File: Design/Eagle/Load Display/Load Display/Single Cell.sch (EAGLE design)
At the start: 12 parts

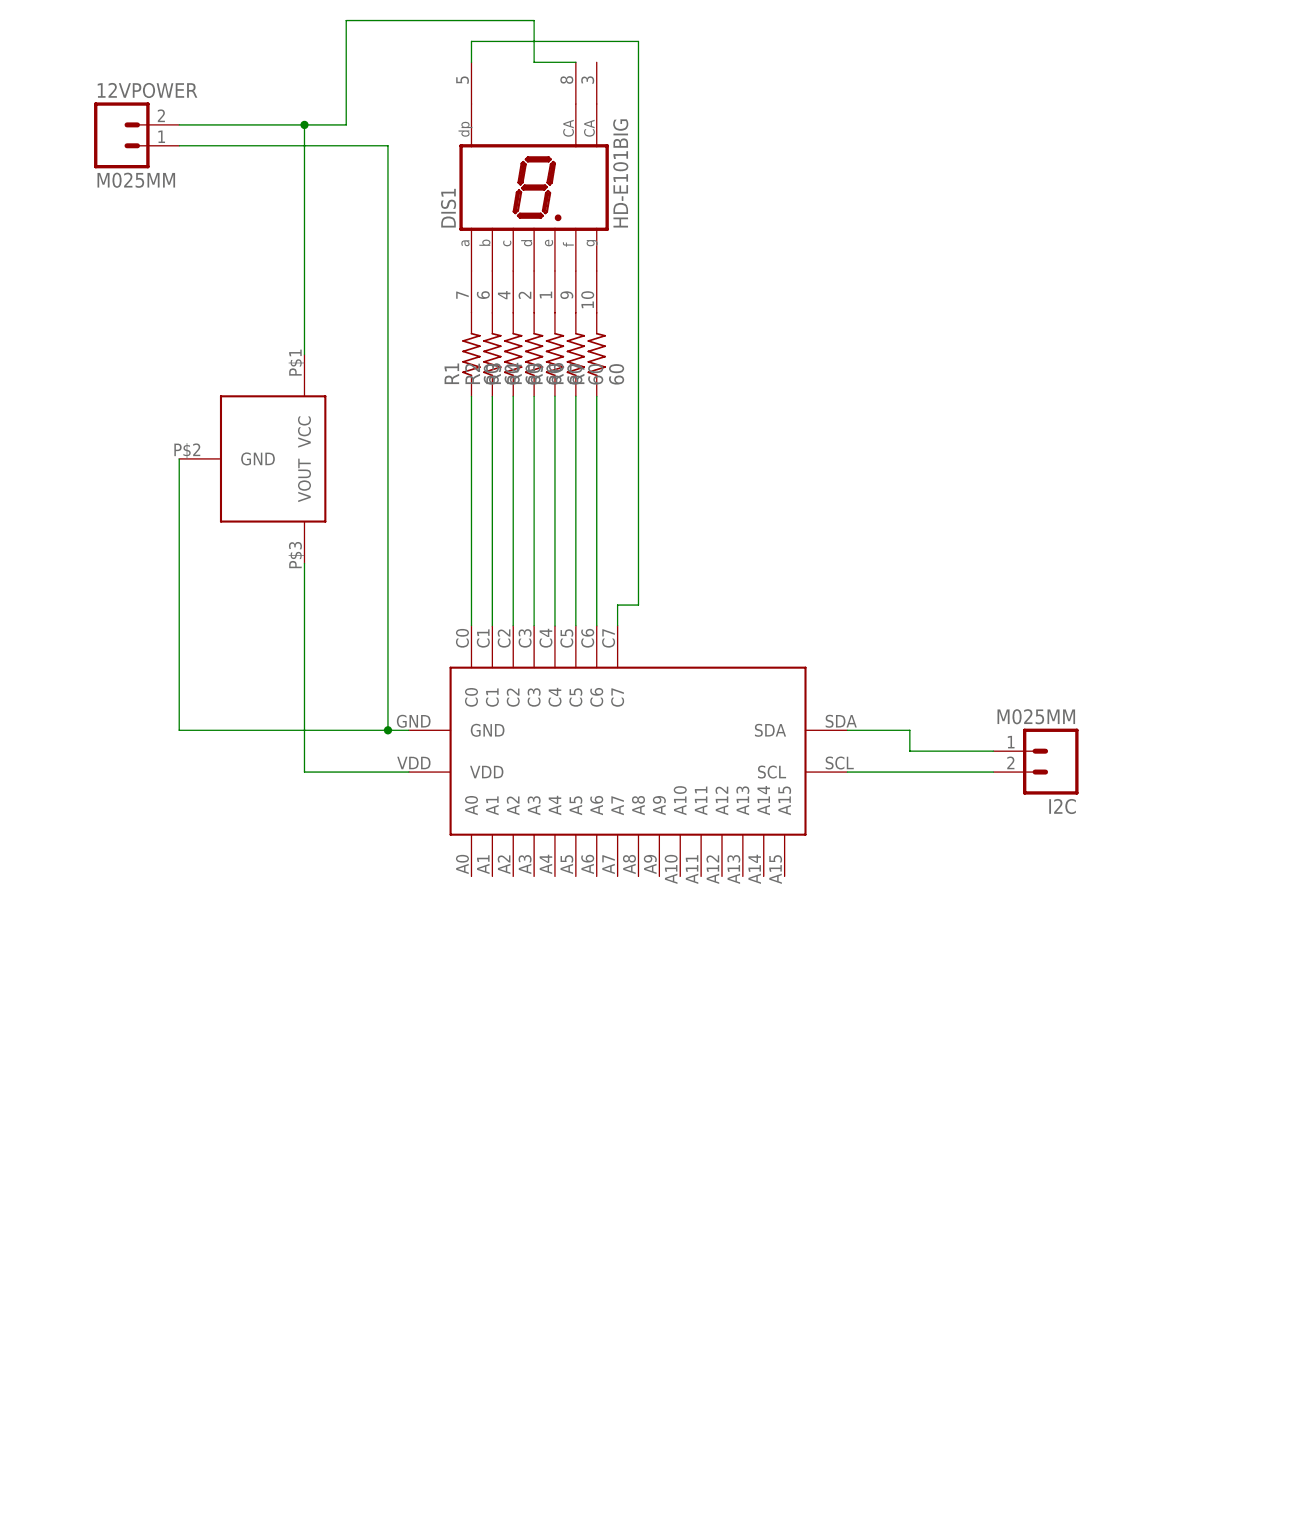
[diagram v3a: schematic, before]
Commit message: Added a bunch of stuff to make the new 7 segment boards.
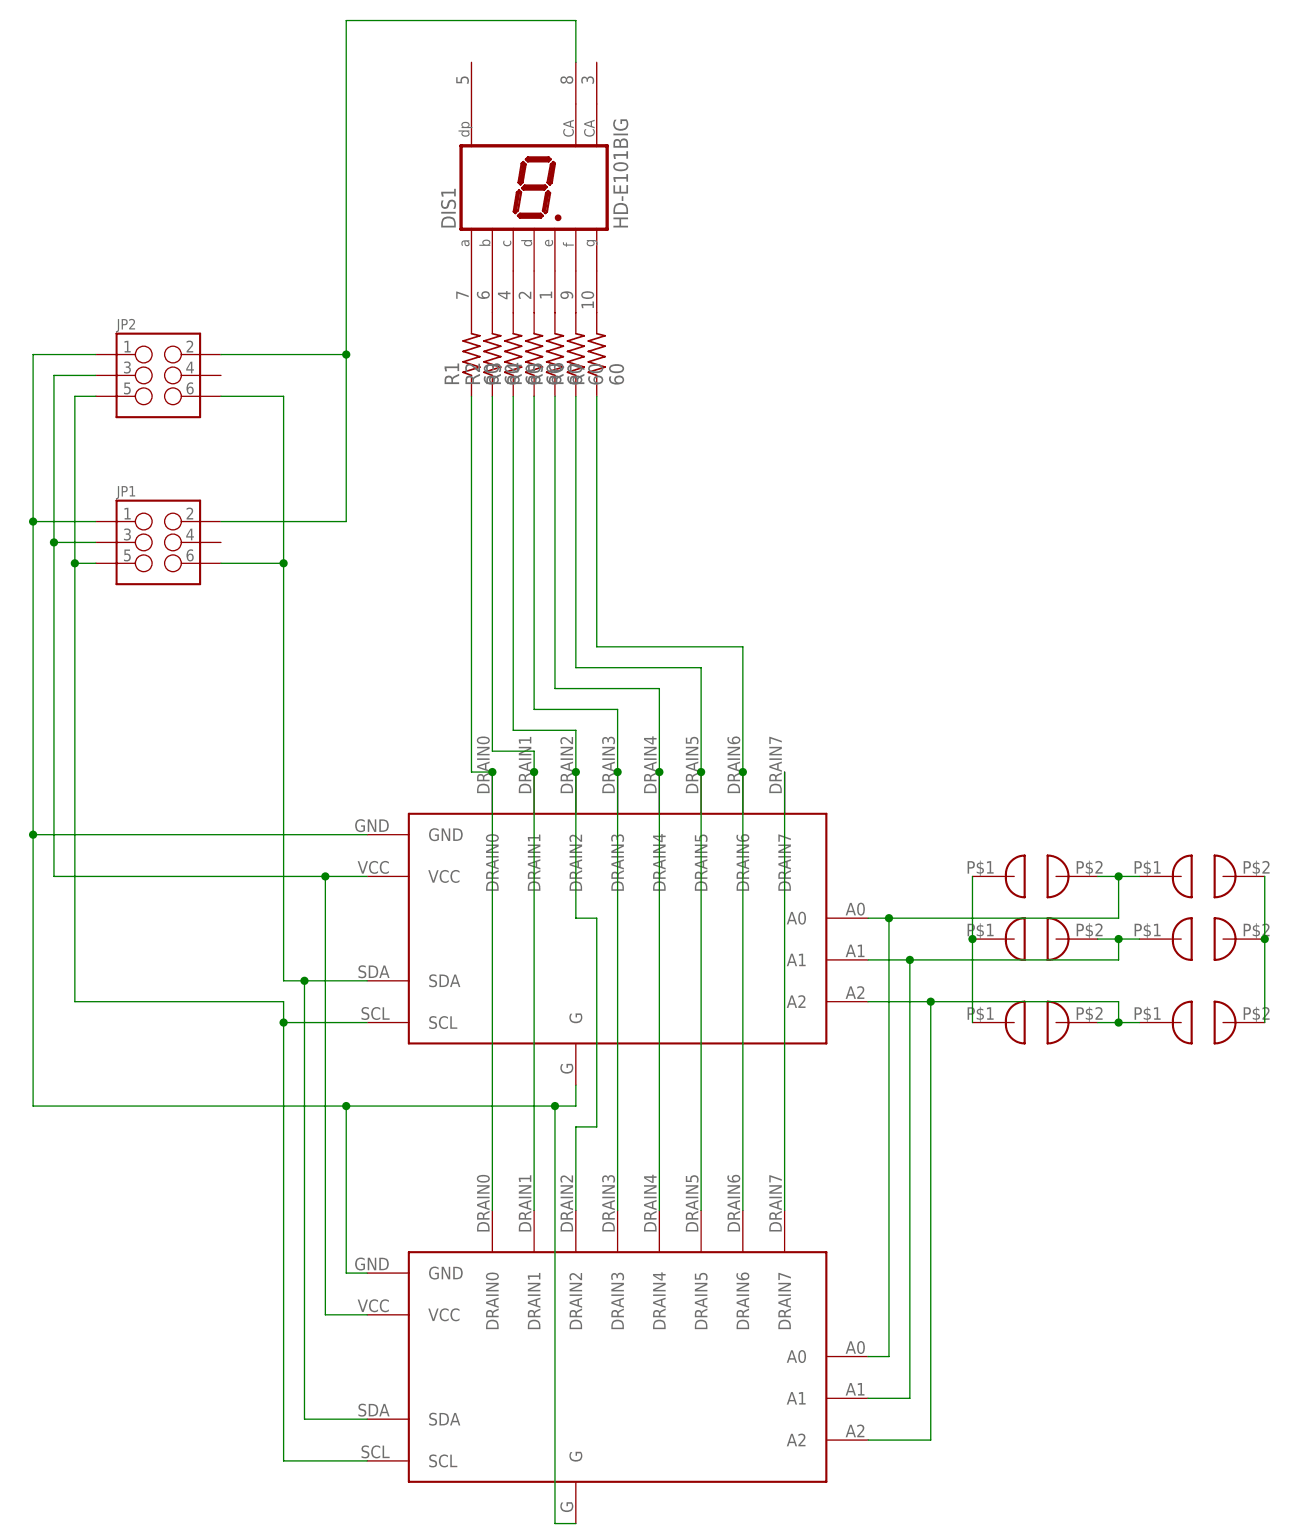
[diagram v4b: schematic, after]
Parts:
- removed 12VPOWER, I2C: M025MM, Ben-SF-Con:M025MM
- added JP1, JP2: (no value), Ben-SF-Con:M03X2SHROUD
- added U$2: (no value), Parts:LED_DRIVERBOARDADAFRUIT
- added U$4, U$5, U$6, U$7: SOLDER_JUMPER, Parts:SOLDER_JUMPER
- added U$8: (no value), Parts:LED_DRIVERBOARD
- DIS1: device Parts:HD-E101BIG -> Parts:HD-E101BACKWARDS
- R1, R2, R3, R4, R5: device Ben-rcl:R-US_0207/10 -> Ben-rcl:R-US_0207/15
- U$1: value 5VREG -> SOLDER_JUMPER; device Parts:5VREG -> Parts:SOLDER_JUMPER
- U$3: value HT16K33BRD -> SOLDER_JUMPER; device Parts:HT16K33BRD -> Parts:SOLDER_JUMPER
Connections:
- removed net N$18: DIS1.DP, U$3.C7
- removed net N$19: U$1.VOUT, U$3.VDD
- removed net N$20: 12VPOWER.2, DIS1.CA@1, U$1.VCC
- new net GND: JP1.1, JP2.1, U$1.P$3, U$2.G, U$2.GND, U$4.P$3, U$6.P$3, U$8.G, U$8.GND
- new net N$29: U$1.P$4, U$2.A0, U$3.P$3, U$8.A0
- new net SDA: JP1.6, JP2.6, U$2.SDA, U$8.SDA
- new net SSCL: JP1.5, JP2.5, U$2.SCL, U$8.SCL
- new net VCC12: DIS1.CA@1, JP1.2, JP2.2
- new net VCC5: JP1.3, JP2.3, U$2.VCC, U$3.P$4, U$5.P$4, U$7.P$4, U$8.VCC
- net N$10: now also U$2.DRAIN2, U$8.DRAIN2; no longer U$3.C2
- net N$11: now also U$2.DRAIN3, U$8.DRAIN3; no longer U$3.C3
- net N$12: now also U$2.DRAIN4, U$8.DRAIN4; no longer U$3.C4
- net N$13: now also U$2.DRAIN5, U$8.DRAIN5; no longer U$3.C5
- net N$14: now also U$2.DRAIN6, U$8.DRAIN6; no longer U$3.C6
- net N$15: now also U$2.A1, U$4.P$4, U$5.P$3, U$8.A1; no longer I2C.1, U$3.SDA
- net N$16: now also U$2.A2, U$6.P$4, U$7.P$3, U$8.A2; no longer I2C.2, U$3.SCL
- net N$17: now also U$2.DRAIN7, U$8.DRAIN7; no longer 12VPOWER.1, U$1.GND, U$3.GND
- net N$8: now also U$2.DRAIN0, U$8.DRAIN0; no longer U$3.C0
- net N$9: now also U$2.DRAIN1, U$8.DRAIN1; no longer U$3.C1

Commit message: Finished the board for the 7 segments.
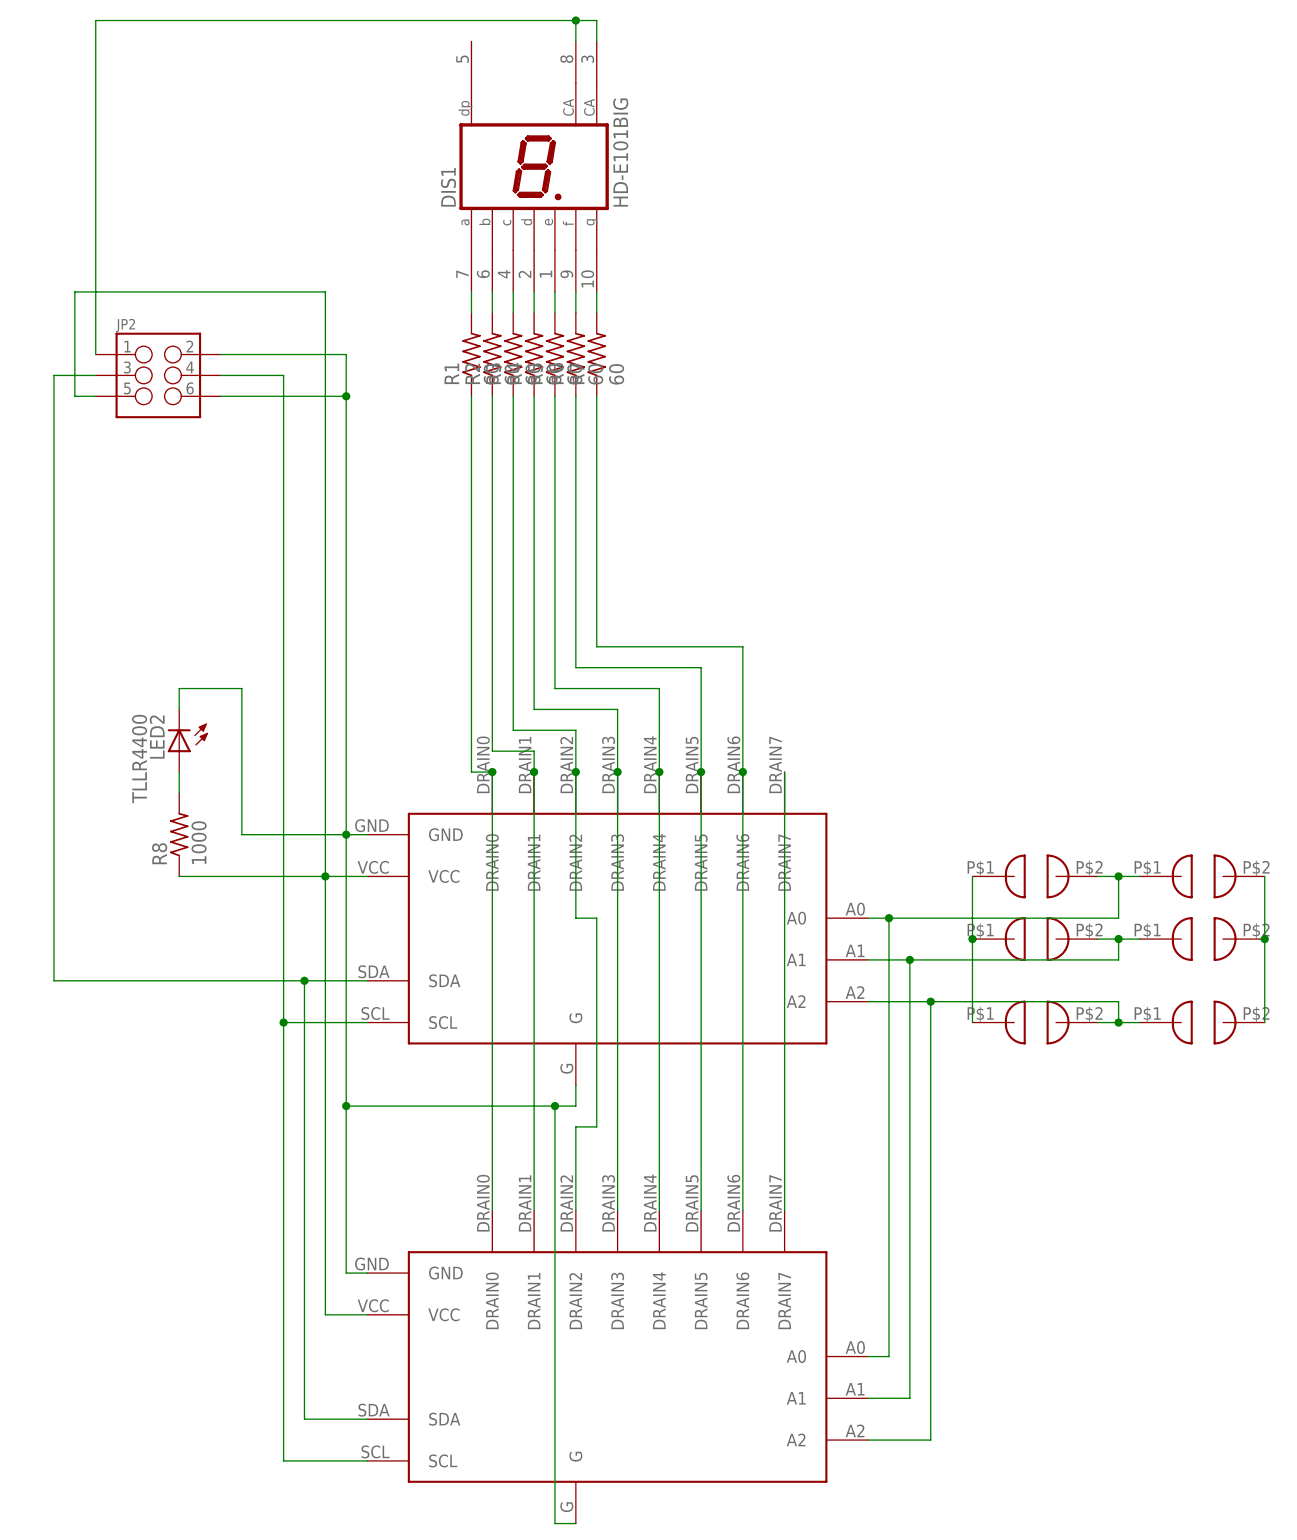
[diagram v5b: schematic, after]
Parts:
- removed JP1: (no value), Ben-SF-Con:M03X2SHROUD
- added LED2: TLLR4400, led:TLLR4400
- added R8: 1000, Ben-rcl:R-US_0207/15
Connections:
- new net N$18: LED2.A, R8.2
- net GND: now also JP2.2, JP2.6, LED2.C; no longer JP1.1, JP2.1
- net SDA: now also JP2.3; no longer JP1.6, JP2.6
- net SSCL: now also JP2.4; no longer JP1.5, JP2.5
- net VCC12: now also DIS1.CA, JP2.1; no longer JP1.2, JP2.2
- net VCC5: now also JP2.5, R8.1; no longer JP1.3, JP2.3
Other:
- moved on the sheet: DIS1
